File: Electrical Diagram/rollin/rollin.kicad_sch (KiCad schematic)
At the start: 5 parts, among them M1 Motor_Servo, U1 L293D

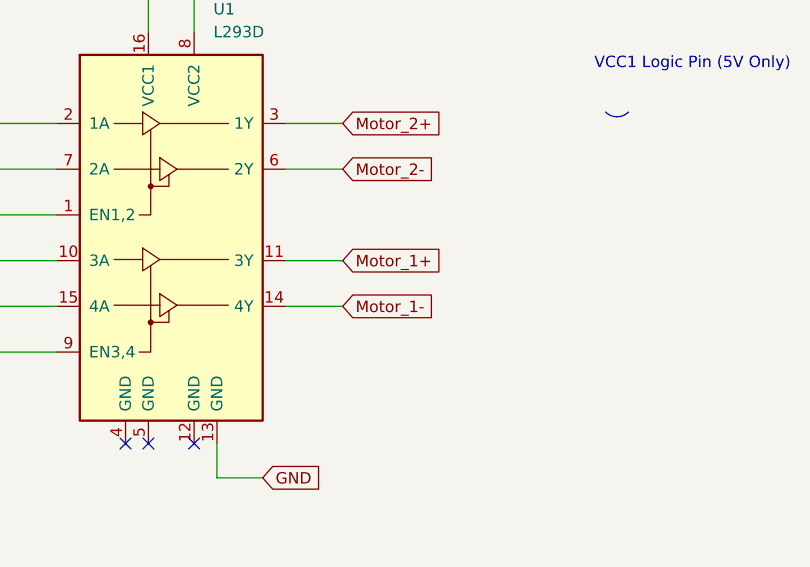
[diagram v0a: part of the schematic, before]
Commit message: Update arduino code for new circuit layout
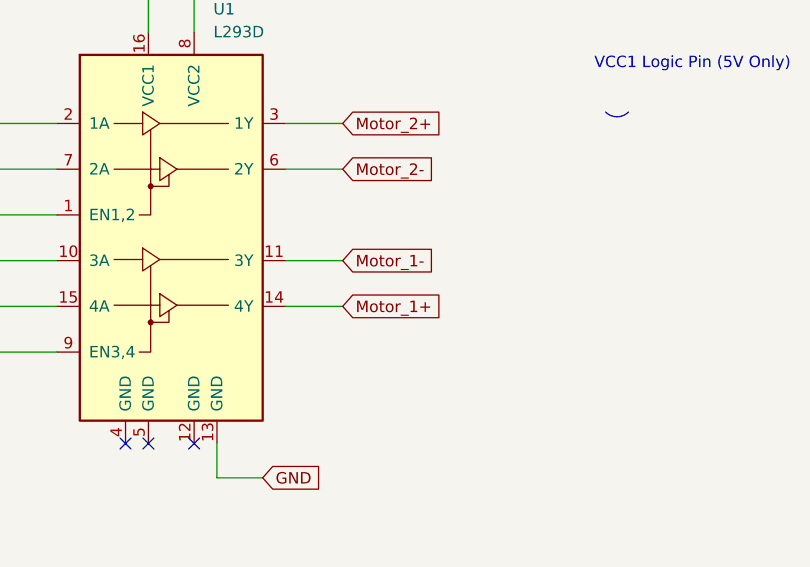
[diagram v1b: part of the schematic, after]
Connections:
- net Motor_1+: now also U1.14 (4Y); no longer U1.11 (3Y)
- net Motor_1-: now also U1.11 (3Y); no longer U1.14 (4Y)

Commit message: Update circuit diagram
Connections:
- net 5v: now also U1.8 (VCC2)
- net 9v: no longer U1.8 (VCC2)
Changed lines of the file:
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@@
 		)
+	)
+	(junction
+		(at 53.34 27.94)
+		(diameter 0)
+		(color 0 0 0 0)
 	)
 	(no_connect
@@
 	(wire
 		(pts
+			(xy 53.34 27.94) (xy 48.26 27.94)
+		)
+		(stroke
+			(width 0)
+			(type default)
+		)
+	)
+	(wire
+		(pts
 			(xy 144.78 64.77) (xy 154.94 64.77)
 		)
@@
 	(wire
 		(pts
+			(xy 53.34 27.94) (xy 53.34 36.83)
+		)
+		(stroke
+			(width 0)
+			(type default)
+		)
+	)
+	(wire
+		(pts
 			(xy 27.94 72.39) (xy 38.1 72.39)
 		)
@@
 	(wire
 		(pts
-			(xy 53.34 30.48) (xy 53.34 36.83)
-		)
-		(stroke
-			(width 0)
-			(type default)
-		)
-	)
-	(wire
-		(pts
 			(xy 55.88 86.36) (xy 55.88 82.55)
 		)
@@
 	(wire
 		(pts
-			(xy 62.23 30.48) (xy 53.34 30.48)
-		)
-		(stroke
-			(width 0)
-			(type default)
-		)
-	)
-	(wire
-		(pts
 			(xy 144.78 62.23) (xy 154.94 62.23)
 		)
@@
 	(wire
 		(pts
-			(xy 62.23 27.94) (xy 48.26 27.94)
+			(xy 62.23 27.94) (xy 53.34 27.94)
 		)
 		(stroke
@@
 			(effects
 				(font
-					(size 1.27 1.27)
-				)
-				(justify left)
-				(hide yes)
-			)
-		)
-	)
-	(global_label "9v"
-		(shape input)
-		(at 62.23 30.48 0)
-		(fields_autoplaced yes)
-		(effects
-			(font
-				(size 1.27 1.27)
-			)
-			(justify left)
-		)
-		(property "Intersheetrefs" "${INTERSHEET_REFS}"
-			(at 67.3923 30.48 0)
-			(effects
-				(font

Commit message: Update arduino code and schematics
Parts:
- removed 9V: Battery_Cell, symbol Device:Battery_Cell
- added BT1: Battery, symbol Device:Battery
- added M2, M3, M4: Motor_DC, symbol Motor:Motor_DC
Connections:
- net 5v: no longer U1.8 (VCC2)
- net 9v: now also U1.8 (VCC2), BT1.1 (+)
- net GND: now also BT1.2 (-)
- net Motor_1+: now also M2.1 (+)
- net Motor_1-: now also M2.2 (-)
- net Motor_2+: now also M3.1 (+), M4.1 (+)
- net Motor_2-: now also M3.2 (-), M4.2 (-)
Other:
- note added: "Motor"
- moved on the sheet: U1

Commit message: update diagram
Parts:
- U1: renamed from HC-SR1; value ~ -> Ultrasonic_sensor
- renumbered U1 to L1
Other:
- note added: "Front Motor"
- note added: "Rear Motor"
- note removed: "Motor"
- moved on the sheet: M3, M4
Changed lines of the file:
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@@
 	)
 	(rectangle
-		(start 87.63 15.24)
+		(start 87.63 46.99)
 		(end 123.19 100.33)
 		(stroke
@@
 		)
 	)
+	(rectangle
+		(start 87.63 15.24)
+		(end 123.19 44.45)
+		(stroke
+			(width 0)
+			(type default)
+		)
+		(fill
+			(type none)
+		)
+	)
 	(arc
 		(start 29.21 69.85)
@@
 	)
 	(rectangle
-		(start 15.24 105.41)
+		(start 15.24 104.14)
 		(end 63.5 134.62)
 		(stroke
@@
 	)
 	(rectangle
-		(start 66.04 105.41)
+		(start 66.04 104.14)
 		(end 87.63 134.62)
 		(stroke
@@
 		)
 	)
-	(text "Motor"
+	(text "Rear Motor"
 		(exclude_from_sim yes)
-		(at 95.758 19.304 0)
+		(at 98.806 19.558 0)
 		(effects
 			(font
@@
 	(text "Launch Mechanism (Servo)\n"
 		(exclude_from_sim yes)
-		(at 39.116 109.982 0)
+		(at 39.116 107.188 0)
+		(effects
+			(font
+				(size 2.032 2.032)
+				(thickness 0.4064)
+				(bold yes)
+			)
+		)
+	)
+	(text "Front Motor"
+		(exclude_from_sim yes)
+		(at 99.06 50.8 0)
 		(effects
 			(font
@@
 	(text "Power"
 		(exclude_from_sim yes)
-		(at 76.454 109.474 0)
+		(at 76.708 107.442 0)
 		(effects
 			(font
@@
 	)
 	(junction
+		(at 170.18 91.44)
+		(diameter 0)
+		(color 0 0 0 0)
+	)
+	(junction
 		(at 68.58 43.18)
 		(diameter 0)
@@
 	(wire
 		(pts
-			(xy 107.95 73.66) (xy 107.95 74.93)
+			(xy 107.95 81.28) (xy 107.95 82.55)
 		)
 		(stroke
@@
 	(wire
 		(pts
-			(xy 170.18 91.44) (xy 171.45 91.44)
+			(xy 170.18 91.44) (xy 180.34 91.44)
 		)
 		(stroke
@@
 	(wire
 		(pts
+			(xy 148.59 82.55) (xy 148.59 91.44)
+		)
+		(stroke
+			(width 0)
+			(type default)
+		)
+	)
+	(wire
+		(pts
 			(xy 29.21 63.5) (xy 39.37 63.5)
 		)
@@
 	(wire
 		(pts
-			(xy 142.24 82.55) (xy 144.78 82.55)
+			(xy 142.24 82.55) (xy 148.59 82.55)
 		)
 		(stroke
@@
 	(wire
 		(pts
-			(xy 107.95 88.9) (xy 107.95 87.63)
+			(xy 107.95 96.52) (xy 107.95 95.25)
 		)
 		(stroke
@@
 	(wire
 		(pts
-			(xy 101.6 64.77) (xy 107.95 64.77)
+			(xy 101.6 72.39) (xy 107.95 72.39)
 		)
 		(stroke
@@
 	(wire
 		(pts
-			(xy 107.95 64.77) (xy 107.95 63.5)
+			(xy 107.95 72.39) (xy 107.95 71.12)
 		)
 		(stroke
@@
 	(wire
 		(pts
-			(xy 101.6 49.53) (xy 107.95 49.53)
+			(xy 101.6 57.15) (xy 107.95 57.15)
 		)
 		(stroke
@@
 	(wire
 		(pts
-			(xy 101.6 88.9) (xy 107.95 88.9)
+			(xy 101.6 96.52) (xy 107.95 96.52)
 		)
 		(stroke
@@
 	(wire
 		(pts
-			(xy 101.6 73.66) (xy 107.95 73.66)
+			(xy 101.6 81.28) (xy 107.95 81.28)
 		)
 		(stroke
@@
 	(wire
 		(pts
-			(xy 107.95 49.53) (xy 107.95 50.8)
+			(xy 107.95 57.15) (xy 107.95 58.42)
+		)
+		(stroke
+			(width 0)
+			(type default)
+		)
+	)
+	(wire
+		(pts
+			(xy 148.59 91.44) (xy 170.18 91.44)
 		)
 		(stroke
@@
 	(global_label "GND"
 		(shape input)
-		(at 171.45 91.44 0)
+		(at 180.34 91.44 0)
 		(fields_autoplaced yes)
 		(effects
@@
 		)
 		(property "Intersheetrefs" "${INTERSHEET_REFS}"
-			(at 178.3057 91.44 0)
+			(at 187.1957 91.44 0)
 			(effects
 				(font
@@
 	(global_label "Motor_2-"
 		(shape input)
-		(at 101.6 64.77 180)
+		(at 101.6 72.39 180)
 		(fields_autoplaced yes)
 		(effects
@@
 		)
 		(property "Intersheetrefs" "${INTERSHEET_REFS}"
-			(at 89.604 64.77 0)
+			(at 89.604 72.39 0)
 			(effects
 				(font
@@
 	(global_label "Motor_3+"
 		(shape input)
-		(at 101.6 73.66 180)
+		(at 101.6 81.28 180)
 		(fields_autoplaced yes)
 		(effects
@@
 		)
 		(property "Intersheetrefs" "${INTERSHEET_REFS}"
-			(at 89.604 73.66 0)
+			(at 89.604 81.28 0)
 			(effects
 				(font
@@
 	(global_label "Motor_2+"
 		(shape input)
-		(at 101.6 49.53 180)
+		(at 101.6 57.15 180)
 		(fields_autoplaced yes)
 		(effects
@@
 		)
 		(property "Intersheetrefs" "${INTERSHEET_REFS}"
-			(at 89.604 49.53 0)
+			(at 89.604 57.15 0)
 			(effects
 				(font
@@
 		)
 	)
-	(global_label "GND"
-		(shape input)
-		(at 144.78 82.55 0)
-		(fields_autoplaced yes)
-		(effects
-			(font
-				(size 1.27 1.27)
-			)
-			(justify left)
-		)
-		(property "Intersheetrefs" "${INTERSHEET_REFS}"
-			(at 151.6357 82.55 0)
-			(effects
-				(font
-					(size 1.27 1.27)
-				)
-				(justify left)
-				(hide yes)
-			)
-		)
-	)
 	(global_label "Motor_3-"
 		(shape input)
-		(at 101.6 88.9 180)
+		(at 101.6 96.52 180)
 		(fields_autoplaced yes)
 		(effects
@@
 		)
 		(property "Intersheetrefs" "${INTERSHEET_REFS}"
-			(at 89.604 88.9 0)
+			(at 89.604 96.52 0)
 			(effects
 				(font
@@
 		(dnp no)
 		(fields_autoplaced yes)
-		(property "Reference" "U1"
+		(property "Reference" "L1"
 			(at 56.7533 25.4 0)
 			(effects
@@
 			(project ""
 				(path "/3285cce8-c68d-4dd9-8308-ce1a0c5ab0a8"
-					(reference "U1")
+					(reference "L1")
 					(unit 1)
 				)
@@
 		(on_board yes)
 		(dnp no)
-		(property "Reference" "HC-SR1"
-			(at 135.128 77.216 90)
+		(property "Reference" "U1"
+			(at 133.858 77.978 90)
 			(effects
 				(font
@@
 			)
 		)
-		(property "Value" "~"
-			(at 134.874 78.486 90)
+		(property "Value" "Ultrasonic_sensor"
+			(at 135.89 86.36 90)
 			(effects
 				(font
@@
 			(project ""
 				(path "/3285cce8-c68d-4dd9-8308-ce1a0c5ab0a8"
-					(reference "HC-SR1")
+					(reference "U1")
 					(unit 1)
 				)
@@
 	(symbol
 		(lib_id "Motor:Motor_DC")
-		(at 107.95 80.01 0)
+		(at 107.95 87.63 0)
 		(unit 1)
 		(exclude_from_sim no)
@@
 		(fields_autoplaced yes)
 		(property "Reference" "M4"
-			(at 113.03 81.2799 0)
+			(at 113.03 88.8999 0)
 			(effects
 				(font
@@
 		)
 		(property "Value" "Motor_DC"
-			(at 113.03 83.8199 0)
+			(at 113.03 91.4399 0)
 			(effects
 				(font
@@
 		)
 		(property "Footprint" ""
-			(at 107.95 82.296 0)
+			(at 107.95 89.916 0)
 			(effects
 				(font
@@
 		)
 		(property "Datasheet" "~"
-			(at 107.95 82.296 0)
+			(at 107.95 89.916 0)
 			(effects
 				(font
@@
 		)
 		(property "Description" "DC Motor"
-			(at 107.95 80.01 0)
+			(at 107.95 87.63 0)
 			(effects
 				(font
@@
 	(symbol
 		(lib_id "Motor:Motor_DC")
-		(at 107.95 55.88 0)
+		(at 107.95 63.5 0)
 		(unit 1)
 		(exclude_from_sim no)
@@
 		(fields_autoplaced yes)
 		(property "Reference" "M3"
-			(at 113.03 57.1499 0)
+			(at 113.03 64.7699 0)
 			(effects
 				(font
@@
 		)
 		(property "Value" "Motor_DC"
-			(at 113.03 59.6899 0)
+			(at 113.03 67.3099 0)
 			(effects
 				(font
@@
 		)
 		(property "Footprint" ""
-			(at 107.95 58.166 0)
+			(at 107.95 65.786 0)
 			(effects
 				(font
@@
 		)
 		(property "Datasheet" "~"
-			(at 107.95 58.166 0)
+			(at 107.95 65.786 0)
 			(effects
 				(font
@@
 		)
 		(property "Description" "DC Motor"
-			(at 107.95 55.88 0)
+			(at 107.95 63.5 0)
 			(effects
 				(font
